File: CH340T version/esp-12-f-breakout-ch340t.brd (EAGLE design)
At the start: 26.7 x 43.3 mm, 22 parts, among them IC1 REG1117, Q1 12.000

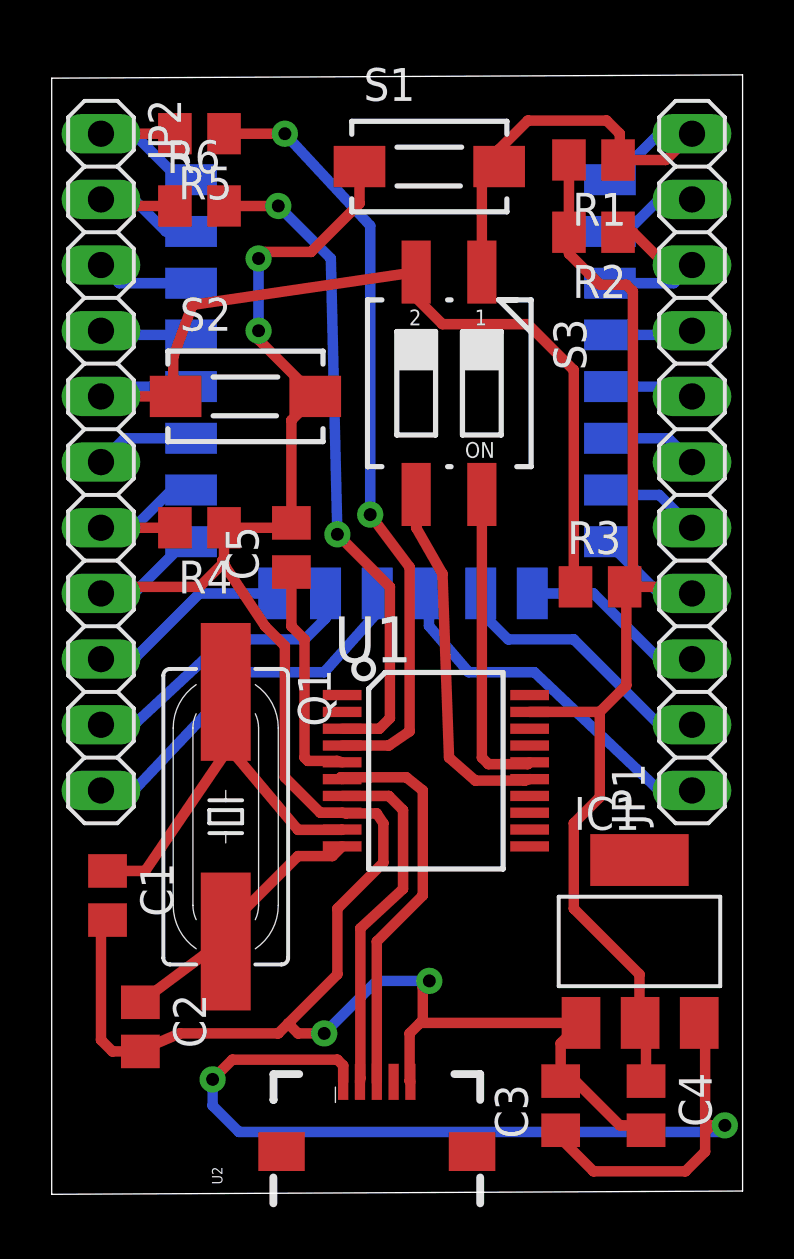
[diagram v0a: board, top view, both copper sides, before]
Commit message: USB +5V pin added to pin headers
- Additional GND pin added
- Stabilizer layout rearranged
- Vias diameter slightly increased
- Drill-aid (0.4 mm) added
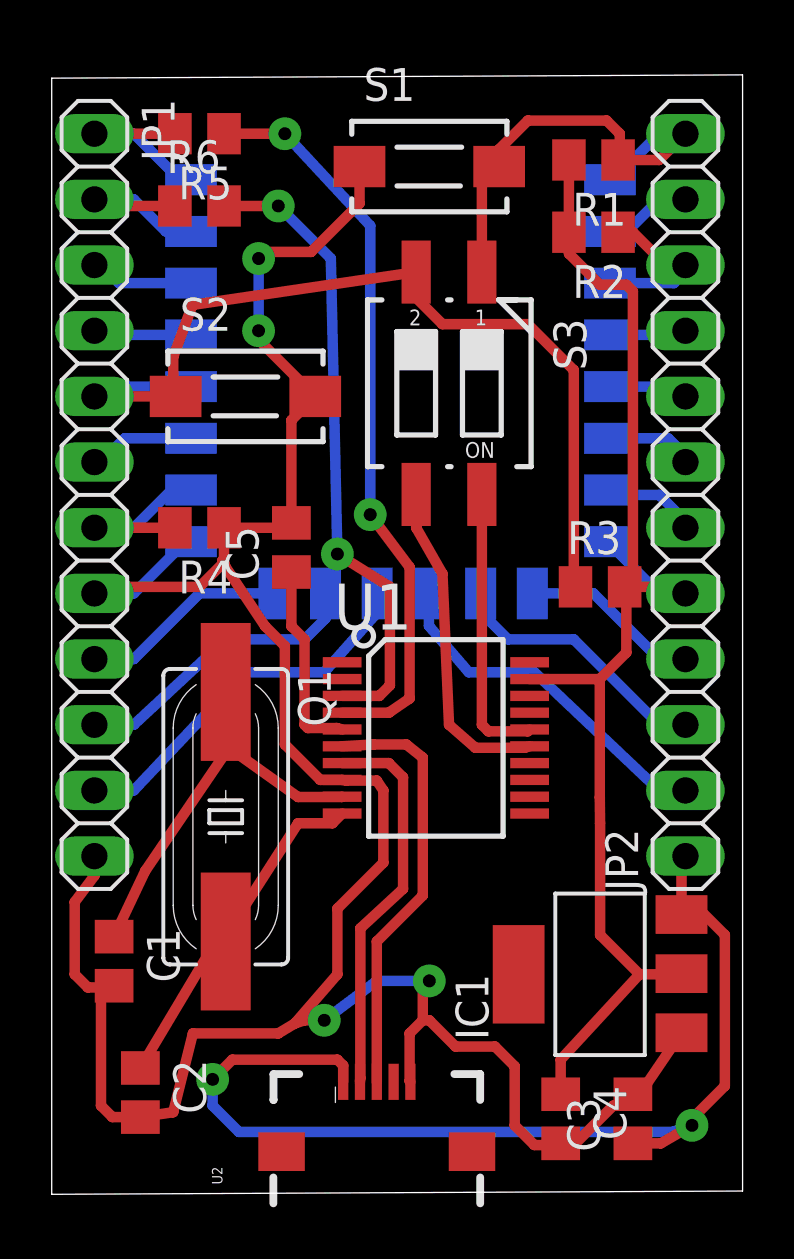
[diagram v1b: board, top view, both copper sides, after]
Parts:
- JP1, JP2: device pinhead:1X11 -> pinhead:1X12
- moved JP1 23.1 mm to (1.27, 26.9), turned to 270 degrees
- moved JP2 22.6 mm to (24.1, 26.9), turned to 90 degrees
- moved C4 3.34 mm to (19.3, 2.79)
- moved C3 2.84 mm to (22.1, 2.79)
- moved C1 2.55 mm to (2.03, 8.89)
- moved C2 2.54 mm to (3.05, 3.81)
- moved IC1 1.98 mm to (20.8, 8.38), turned to 90 degrees
- moved U1 1.27 mm to (14.5, 17.5)
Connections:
- removed net N$27: C3.1, IC1.3, U2.VBUS1
- new net VUSB: C3.1, IC1.3, JP2.1, U2.VBUS1
- net +3V3: now also JP2.5; no longer JP1.4
- net GND: now also JP1.12, JP1.8; no longer JP2.8
- net N$1: now also JP2.12; no longer JP1.11
- net N$11: now also JP2.3; no longer JP1.2
- net N$12: now also JP1.9; no longer JP2.9
- net N$13: now also JP1.10; no longer JP2.10
- net N$14: now also JP1.11; no longer JP2.11
- net N$15: now also JP2.2; no longer JP1.1
- net N$16: now also JP1.7; no longer JP2.7
- net N$17: now also JP1.6; no longer JP2.6
- net N$18: now also JP1.5; no longer JP2.5
- net N$19: now also JP1.4; no longer JP2.4
- net N$2: now also JP2.11; no longer JP1.10
- net N$20: now also JP1.3; no longer JP2.3
- net N$21: now also JP1.2; no longer JP2.2
- net N$22: now also JP1.1; no longer JP2.1
- net N$3: now also JP2.10; no longer JP1.9
- net N$4: now also JP2.9; no longer JP1.8
- net N$5: now also JP2.8; no longer JP1.7
- net N$6: now also JP2.7; no longer JP1.6
- net N$7: now also JP2.6; no longer JP1.5
- net N$8: now also JP2.4; no longer JP1.3
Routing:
- net VUSB: track 0.00 -> 41.6 mm, vias 0 -> 2
- net N$27: track 40.1 -> 0.00 mm, vias 2 -> 0
- net GND: track 91.0 -> 102.3 mm
- net N$24: track 10.3 -> 13.2 mm
- net +3V3: track 48.9 -> 50.9 mm
- net V3: track 8.90 -> 7.63 mm
- net TXD: track 30.5 -> 29.2 mm
- net RESET: track 12.2 -> 10.9 mm
- net N$25: track 13.8 -> 15.1 mm
- net GPIO0: track 13.9 -> 12.6 mm
- net N$26: track 15.4 -> 16.6 mm
- net RXD: track 25.6 -> 24.6 mm
- net N$1: track 18.6 -> 18.1 mm
- net N$18: track 35.6 -> 36.2 mm
- net N$22: track 7.08 -> 7.59 mm
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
